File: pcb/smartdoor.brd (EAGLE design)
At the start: 34 x 59.7 mm, 5 parts, among them X1 MKDSN1,5/2-5,08, X2 MKDSN1,5/2-5,08

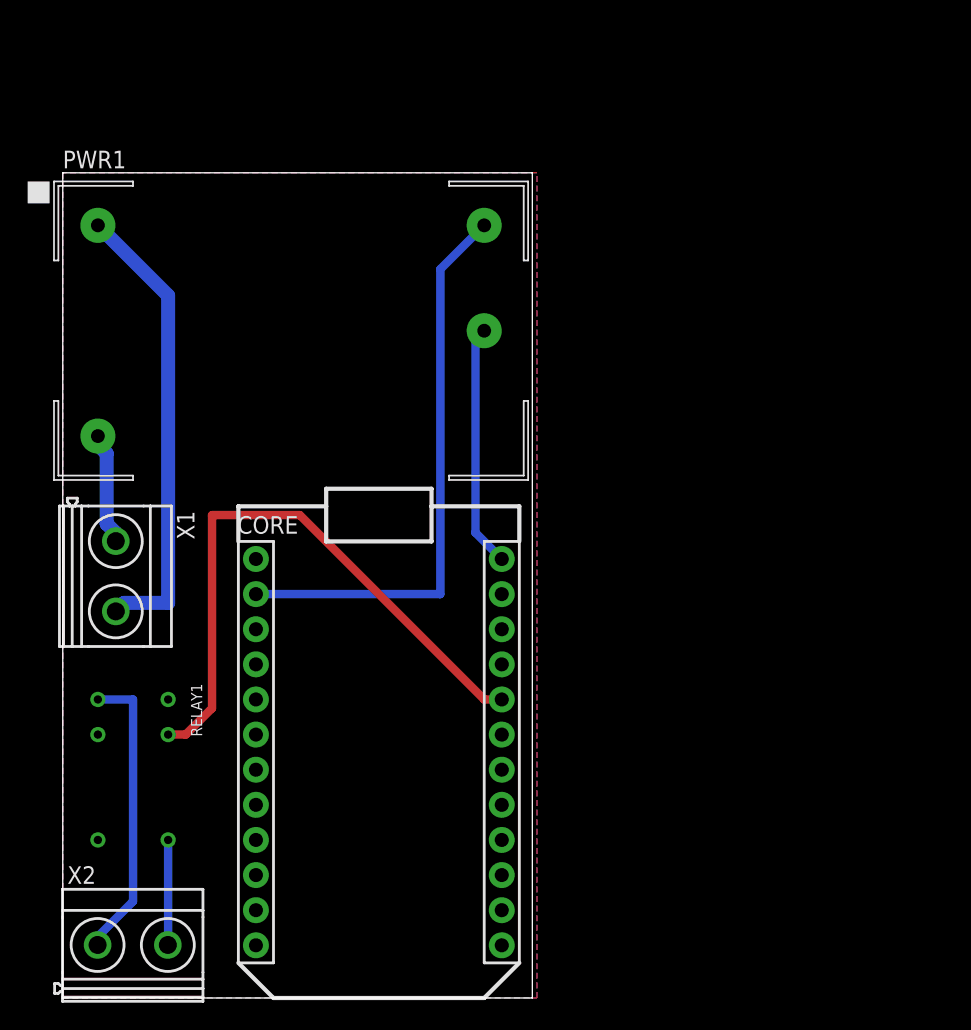
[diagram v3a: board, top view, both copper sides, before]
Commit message: fixed connecting V- of recom with GND mass, updated larger pads for zettler relay in board
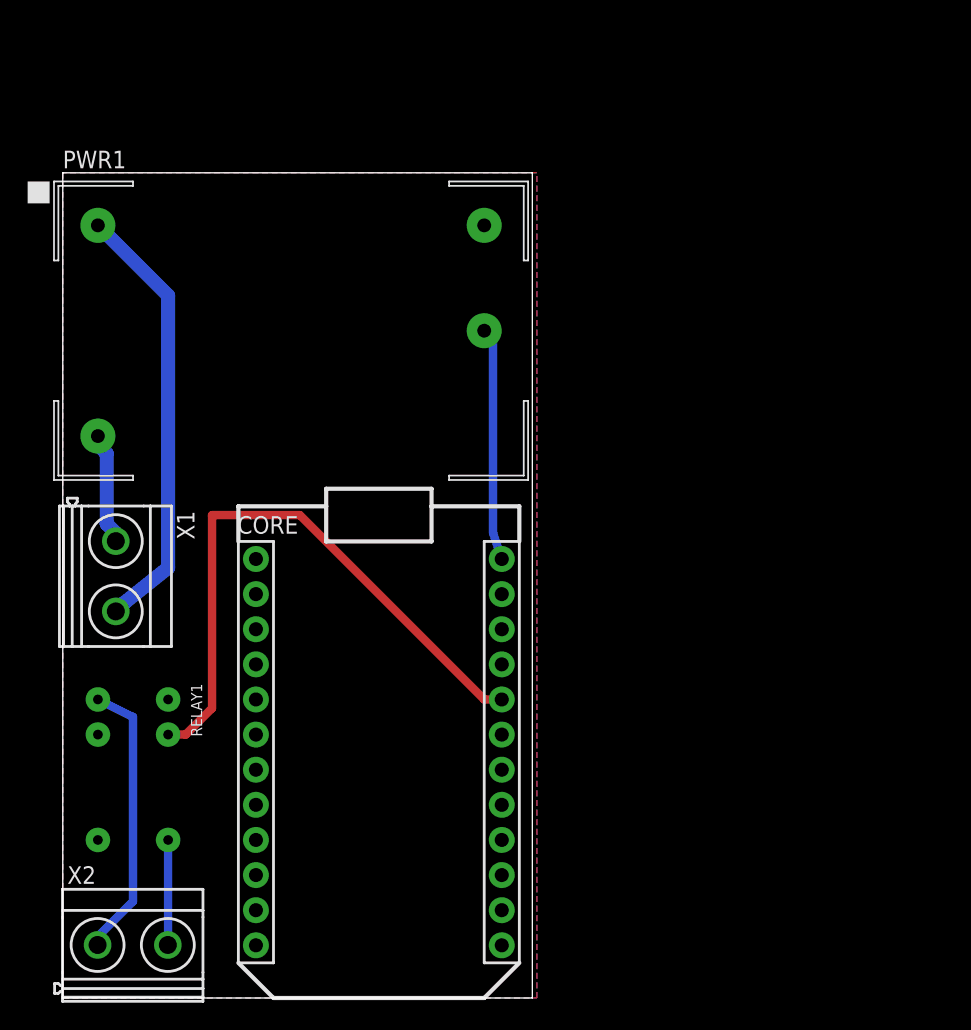
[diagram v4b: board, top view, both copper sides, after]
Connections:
- removed net N$1: CORE.2, PWR1.P3
- net GND: now also CORE.2, PWR1.P3
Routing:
- net N$1: track 41.3 -> 0.00 mm
- net N: track 33.8 -> 32.2 mm
- net LOAD-: track 21.3 -> 20.4 mm
- net 3V3: track 17.6 -> 16.9 mm
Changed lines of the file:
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@@
 <?xml version="1.0" encoding="utf-8"?>
 <!DOCTYPE eagle SYSTEM "eagle.dtd">
-<eagle version="8.2.0">
+<eagle version="8.2.1">
 <drawing>
 <settings>
@@
 <signal name="GND">
 <contactref element="CORE" pad="21"/>
-<contactref element="RELAY1" pad="9"/>
-<polygon width="0.254" layer="16" isolate="0.4064">
+<polygon width="0.6096" layer="16" isolate="0.4064">
 <vertex x="0" y="0"/>
 <vertex x="34.29" y="0"/>
@@
 <vertex x="0" y="59.69"/>
 </polygon>
-<polygon width="0.254" layer="1" isolate="0.4064">
+<polygon width="0.6096" layer="1" isolate="0.4064">
 <vertex x="0" y="0"/>
 <vertex x="34.29" y="0"/>
@@
 <vertex x="0" y="59.69"/>
 </polygon>
+<contactref element="RELAY1" pad="9"/>
+<contactref element="CORE" pad="2"/>
+<contactref element="PWR1" pad="P3"/>
 </signal>
 <signal name="N" class="1">
 <contactref element="PWR1" pad="P1"/>
 <contactref element="X1" pad="2"/>
-<wire x1="7.62" y1="28.575" x2="4.445" y2="28.575" width="1.016" layer="16"/>
-<wire x1="7.62" y1="50.8" x2="7.62" y2="28.575" width="1.016" layer="16"/>
+<wire x1="7.62" y1="31.115" x2="4.445" y2="28.575" width="1.016" layer="16"/>
+<wire x1="7.62" y1="50.8" x2="7.62" y2="31.115" width="1.016" layer="16"/>
 <wire x1="3.175" y1="55.245" x2="7.62" y2="50.8" width="1.016" layer="16"/>
 <wire x1="2.54" y1="55.245" x2="3.175" y2="55.245" width="1.016" layer="16"/>
@@
 <contactref element="PWR1" pad="P4"/>
 <contactref element="CORE" pad="24"/>
-<wire x1="29.845" y1="33.655" x2="31.75" y2="31.75" width="0.6096" layer="16"/>
-<wire x1="29.845" y1="47.625" x2="29.845" y2="33.655" width="0.6096" layer="16"/>
-<wire x1="30.48" y1="48.26" x2="29.845" y2="47.625" width="0.6096" layer="16"/>
+<wire x1="31.115" y1="33.655" x2="31.75" y2="31.75" width="0.6096" layer="16"/>
+<wire x1="31.115" y1="47.625" x2="31.115" y2="33.655" width="0.6096" layer="16"/>
+<wire x1="30.48" y1="48.26" x2="31.115" y2="47.625" width="0.6096" layer="16"/>
 </signal>
 <signal name="LOAD+">
@@
 <contactref element="RELAY1" pad="1"/>
 <contactref element="X2" pad="1"/>
-<wire x1="5.08" y1="21.59" x2="2.54" y2="21.59" width="0.6096" layer="16"/>
-<wire x1="5.08" y1="6.985" x2="5.08" y2="21.59" width="0.6096" layer="16"/>
+<wire x1="5.08" y1="20.32" x2="2.54" y2="21.59" width="0.6096" layer="16"/>
+<wire x1="5.08" y1="6.985" x2="5.08" y2="20.32" width="0.6096" layer="16"/>
 <wire x1="2.54" y1="4.445" x2="5.08" y2="6.985" width="0.6096" layer="16"/>
 <wire x1="2.54" y1="4.445" x2="2.5189" y2="3.835" width="0.6096" layer="16"/>
@@
 <wire x1="31.75" y1="21.59" x2="30.48" y2="21.59" width="0.6096" layer="1"/>
 </signal>
-<signal name="N$1">
-<contactref element="PWR1" pad="P3"/>
-<contactref element="CORE" pad="2"/>
-<wire x1="27.305" y1="29.21" x2="13.97" y2="29.21" width="0.6096" layer="16"/>
-<wire x1="27.305" y1="52.705" x2="27.305" y2="29.21" width="0.6096" layer="16"/>
-<wire x1="30.48" y1="55.88" x2="27.305" y2="52.705" width="0.6096" layer="16"/>
+<signal name="VOUT-">
 </signal>
 </signals>

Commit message: fixed mirrored relay
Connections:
- net LOAD+: now also RELAY1.5; no longer RELAY1.6
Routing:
- net LOAD+: track 7.60 -> 9.17 mm
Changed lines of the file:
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@@
 <vertex x="0" y="59.69"/>
 </polygon>
-<contactref element="RELAY1" pad="9"/>
 <contactref element="CORE" pad="2"/>
 <contactref element="PWR1" pad="P3"/>
+<contactref element="RELAY1" pad="9"/>
 </signal>
 <signal name="N" class="1">
@@
 <wire x1="30.48" y1="48.26" x2="31.115" y2="47.625" width="0.6096" layer="16"/>
 </signal>
-<signal name="LOAD+">
-<contactref element="RELAY1" pad="6"/>
-<contactref element="X2" pad="2"/>
-<wire x1="7.62" y1="4.445" x2="7.62" y2="11.43" width="0.6096" layer="16"/>
-<wire x1="7.62" y1="4.445" x2="7.5989" y2="3.835" width="0.6096" layer="16"/>
-</signal>
-<signal name="LOAD-">
-<contactref element="RELAY1" pad="1"/>
-<contactref element="X2" pad="1"/>
-<wire x1="5.08" y1="20.32" x2="2.54" y2="21.59" width="0.6096" layer="16"/>
-<wire x1="5.08" y1="6.985" x2="5.08" y2="20.32" width="0.6096" layer="16"/>
-<wire x1="2.54" y1="4.445" x2="5.08" y2="6.985" width="0.6096" layer="16"/>
-<wire x1="2.54" y1="4.445" x2="2.5189" y2="3.835" width="0.6096" layer="16"/>
-</signal>
 <signal name="SWITCH">
 <contactref element="CORE" pad="20"/>
@@
 <signal name="VOUT-">
 </signal>
+<signal name="LOAD-">
+<contactref element="RELAY1" pad="1"/>
+<contactref element="X2" pad="1"/>
+<wire x1="6.82625" y1="20.79625" x2="7.62" y2="21.59" width="0.6096" layer="16"/>
+<wire x1="6.6675" y1="20.79625" x2="6.82625" y2="20.79625" width="0.6096" layer="16"/>
+<wire x1="5.23875" y1="19.3675" x2="6.6675" y2="20.79625" width="0.6096" layer="16"/>
+<wire x1="5.23875" y1="6.985" x2="5.23875" y2="19.3675" width="0.6096" layer="16"/>
+<wire x1="2.54" y1="4.28625" x2="5.23875" y2="6.985" width="0.6096" layer="16"/>
+<wire x1="2.54" y1="3.96875" x2="2.54" y2="4.28625" width="0.6096" layer="16"/>
+<wire x1="2.54" y1="3.96875" x2="2.5189" y2="3.835" width="0.6096" layer="16"/>
+</signal>
+<signal name="LOAD+">
+<contactref element="RELAY1" pad="5"/>
+<contactref element="X2" pad="2"/>
+<wire x1="7.62" y1="11.1125" x2="7.62" y2="11.43" width="0.6096" layer="16"/>
+<wire x1="9.525" y1="9.2075" x2="7.62" y2="11.1125" width="0.6096" layer="16"/>
+<wire x1="9.525" y1="6.19125" x2="9.525" y2="9.2075" width="0.6096" layer="16"/>
+<wire x1="7.62" y1="4.28625" x2="9.525" y2="6.19125" width="0.6096" layer="16"/>
+<wire x1="7.62" y1="3.96875" x2="7.62" y2="4.28625" width="0.6096" layer="16"/>
+<wire x1="7.62" y1="3.96875" x2="7.5989" y2="3.835" width="0.6096" layer="16"/>
+</signal>
 </signals>
